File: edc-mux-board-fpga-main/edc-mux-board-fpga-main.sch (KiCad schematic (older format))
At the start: 4 parts

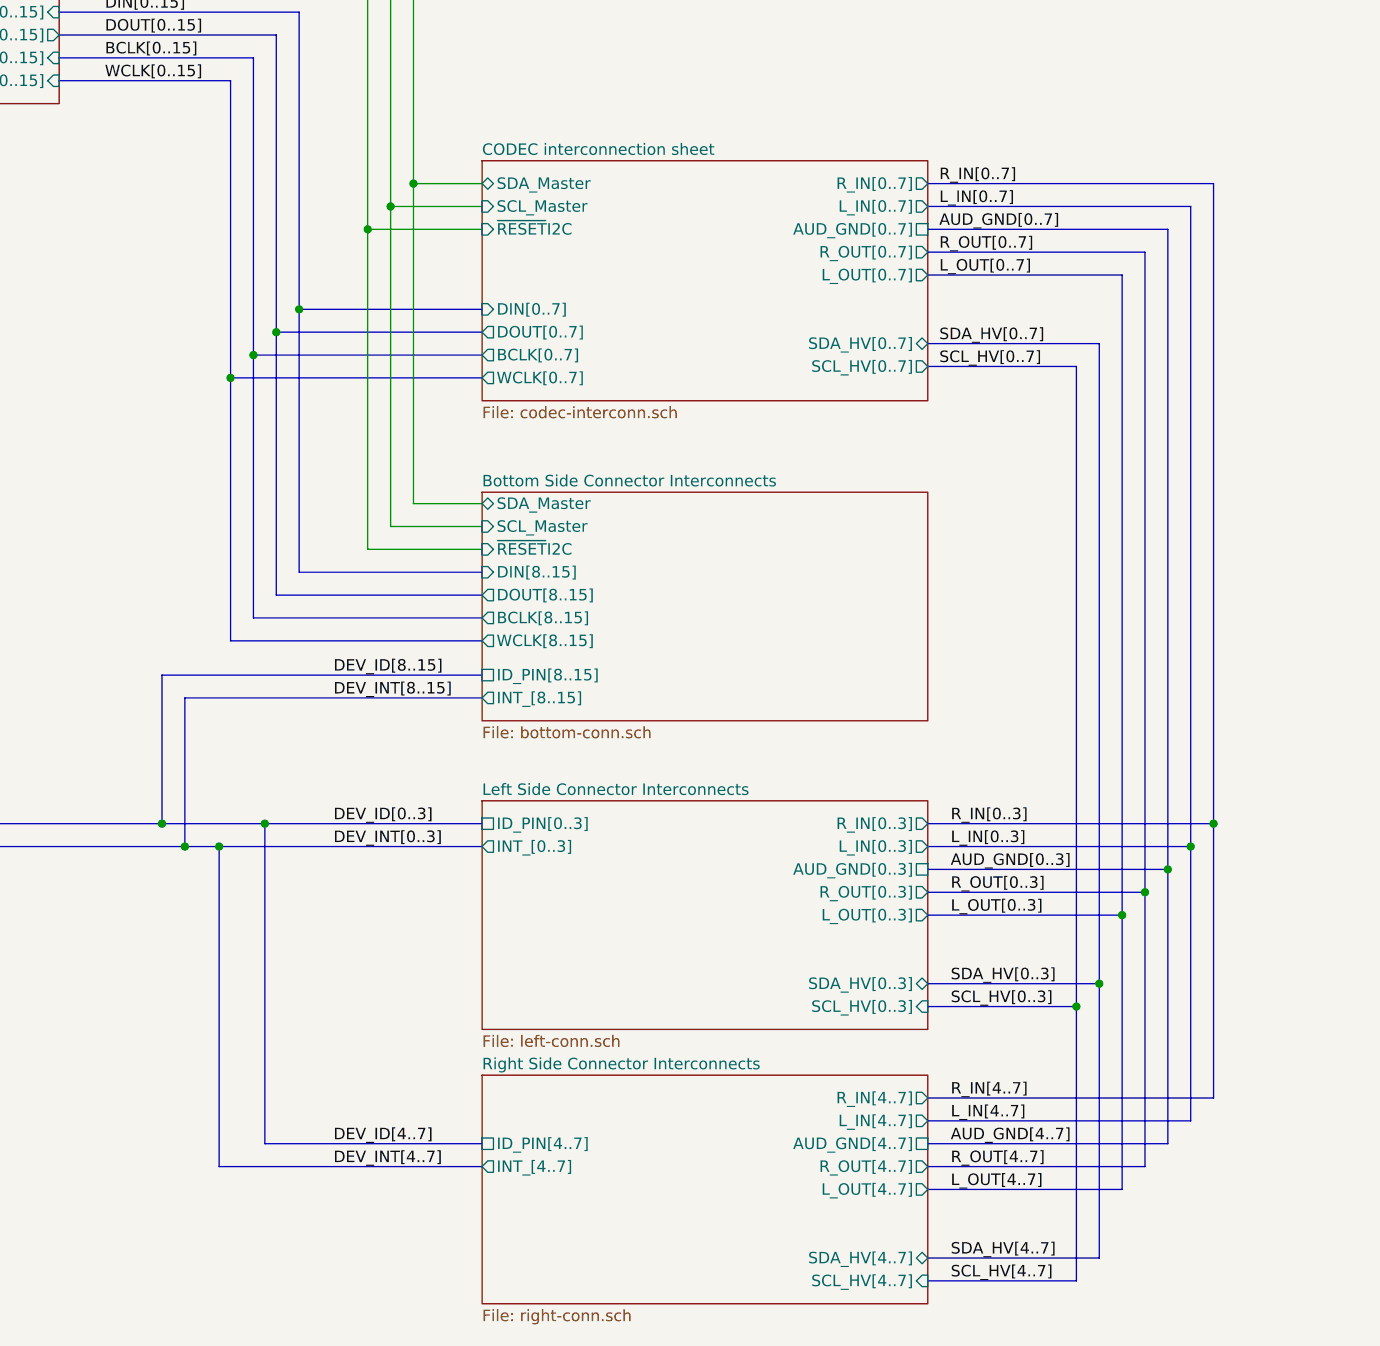
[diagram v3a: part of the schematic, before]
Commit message: testing migration of device connectors and ESD diodes into conn.sch
This means that I can't have the values of the connectors be the device number but hopefully it will allow me to utilize the schematic duplication features with the connectors and diodes
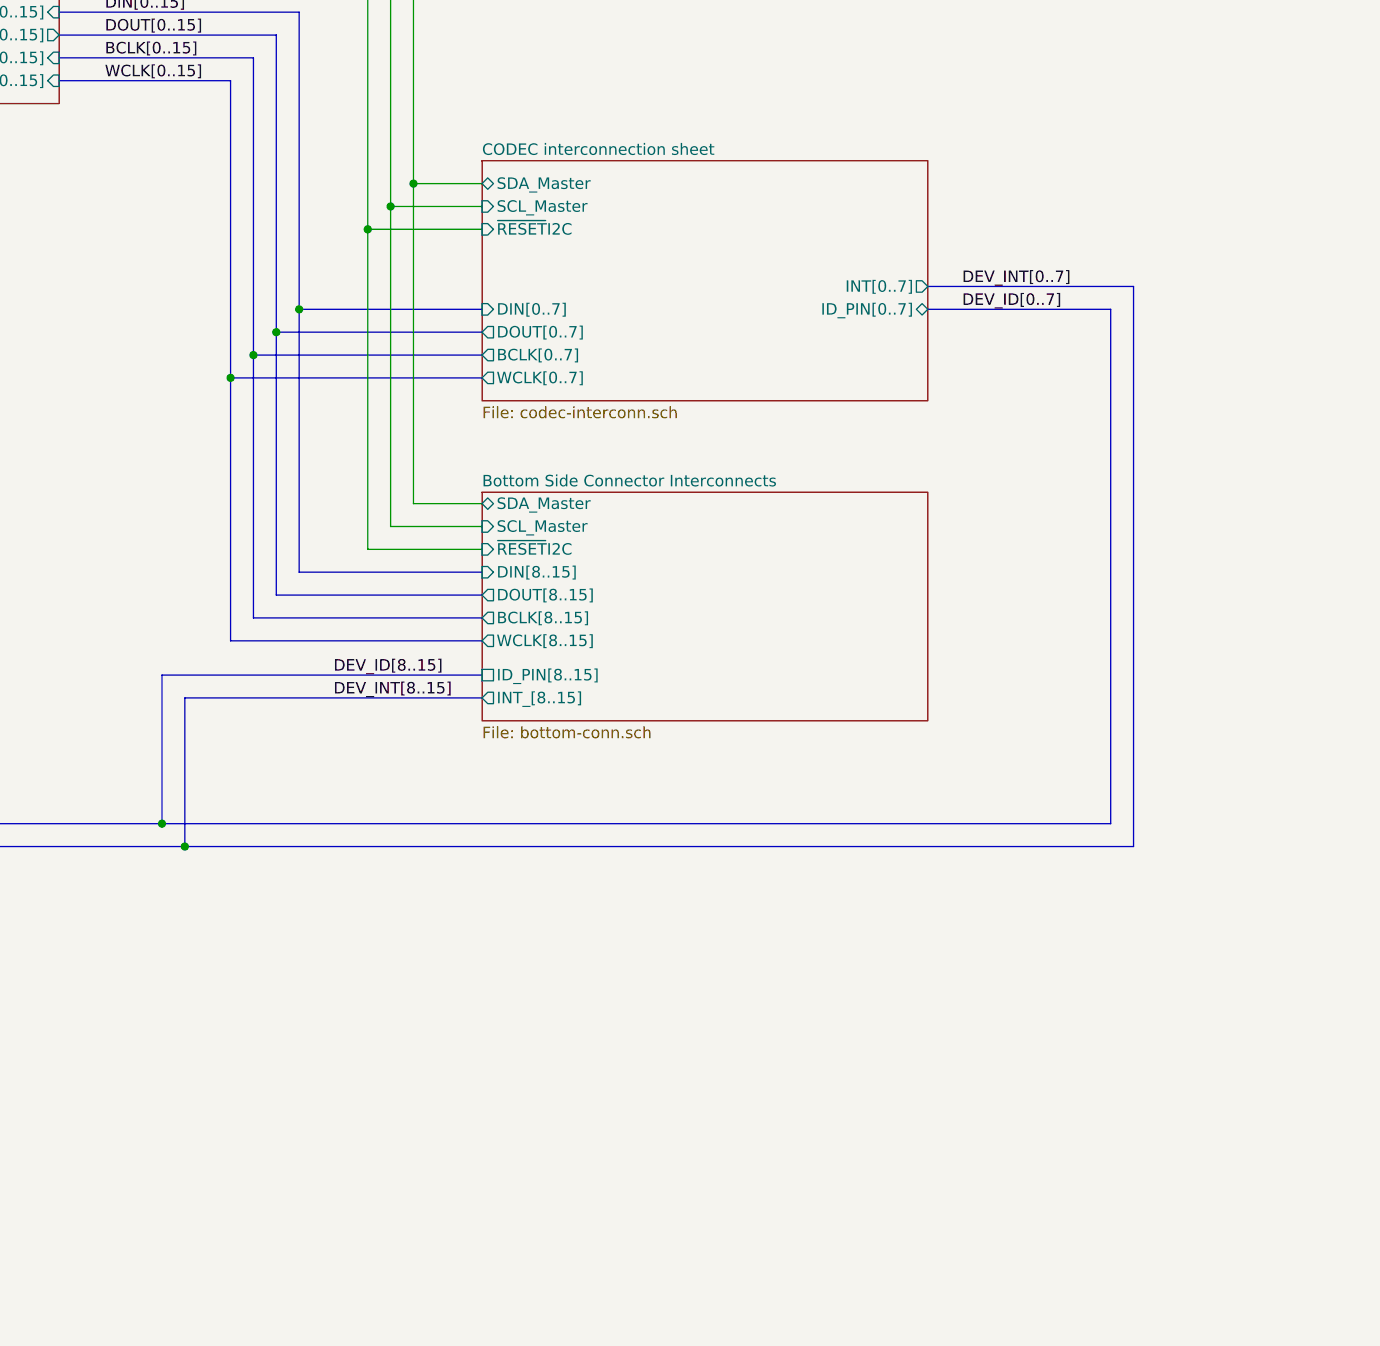
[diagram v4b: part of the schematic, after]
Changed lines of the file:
@@
 $Descr USLedger 17000 11000
 encoding utf-8
-Sheet 1 19
+Sheet 1 17
 Title "EDC Mux Board"
 Date "2019-05-17"
@@
 F4 "BCLK[0..7]" O L 4900 6050 50
 F5 "WCLK[0..7]" O L 4900 6150 50
-F6 "L_OUT[0..7]" O R 6850 5700 50
-F7 "R_OUT[0..7]" O R 6850 5600 50
-F8 "AUD_GND[0..7]" U R 6850 5500 50
-F9 "R_IN[0..7]" O R 6850 5300 50
-F10 "L_IN[0..7]" O R 6850 5400 50
-F11 "SCL_Master" I L 4900 5400 50
-F12 "SDA_Master" B L 4900 5300 50
-F13 "~RESET~I2C" I L 4900 5500 50
-F14 "SDA_HV[0..7]" B R 6850 6000 50
-F15 "SCL_HV[0..7]" O R 6850 6100 50
-$EndSheet
-$Sheet
-S 4900 8000 1950 1000
-U 5CBF625C
-F0 "Left Side Connector Interconnects" 50
-F1 "left-conn.sch" 50
-F2 "R_IN[0..3]" O R 6850 8100 50
-F3 "L_IN[0..3]" O R 6850 8200 50
-F4 "AUD_GND[0..3]" U R 6850 8300 50
-F5 "SDA_HV[0..3]" B R 6850 8800 50
-F6 "SCL_HV[0..3]" I R 6850 8900 50
-F7 "L_OUT[0..3]" O R 6850 8500 50
-F8 "R_OUT[0..3]" O R 6850 8400 50
-F9 "ID_PIN[0..3]" U L 4900 8100 50
-F10 "INT_[0..3]" O L 4900 8200 50
-$EndSheet
-$Sheet
-S 4900 9200 1950 1000
-U 5CBF628A
-F0 "Right Side Connector Interconnects" 50
-F1 "right-conn.sch" 50
-F2 "R_IN[4..7]" O R 6850 9300 50
-F3 "L_IN[4..7]" O R 6850 9400 50
-F4 "AUD_GND[4..7]" U R 6850 9500 50
-F5 "SDA_HV[4..7]" B R 6850 10000 50
-F6 "SCL_HV[4..7]" I R 6850 10100 50
-F7 "L_OUT[4..7]" O R 6850 9700 50
-F8 "R_OUT[4..7]" O R 6850 9600 50
-F9 "ID_PIN[4..7]" U L 4900 9500 50
-F10 "INT_[4..7]" O L 4900 9600 50
+F6 "SCL_Master" I L 4900 5400 50
+F7 "SDA_Master" B L 4900 5300 50
+F8 "~RESET~I2C" I L 4900 5500 50
+F9 "ID_PIN[0..7]" B R 6850 5850 50
+F10 "INT[0..7]" O R 6850 5750 50
 $EndSheet
 Text Notes 17350 6950 0    50   ~ 0
@@
 	3800 6150 4900 6150
 Wire Bus Line
-	6850 5300 8100 5300
-Wire Bus Line
-	6850 5400 8000 5400
-Wire Bus Line
-	6850 5500 7900 5500
-Wire Bus Line
-	6850 5600 7800 5600
-Wire Bus Line
-	6850 5700 7700 5700
-Wire Bus Line
-	6850 6000 7600 6000
-Wire Bus Line
-	6850 6100 7500 6100
-Wire Bus Line
 	900  8100 3500 8100
 Wire Bus Line
@@
 Wire Bus Line
 	800  8200 800  4750
-Text Label 6900 5300 0    50   ~ 0
-R_IN[0..7]
-Text Label 6900 5400 0    50   ~ 0
-L_IN[0..7]
-Text Label 6900 5500 0    50   ~ 0
-AUD_GND[0..7]
-Text Label 6900 5600 0    50   ~ 0
-R_OUT[0..7]
-Text Label 6900 5700 0    50   ~ 0
-L_OUT[0..7]
-Text Label 6900 6000 0    50   ~ 0
-SDA_HV[0..7]
-Text Label 6900 6100 0    50   ~ 0
-SCL_HV[0..7]
-Text Label 6950 8900 0    50   ~ 0
-SCL_HV[0..3]
-Text Label 6950 8800 0    50   ~ 0
-SDA_HV[0..3]
-Text Label 6950 8500 0    50   ~ 0
-L_OUT[0..3]
-Text Label 6950 8400 0    50   ~ 0
-R_OUT[0..3]
-Text Label 6950 8300 0    50   ~ 0
-AUD_GND[0..3]
-Text Label 6950 8200 0    50   ~ 0
-L_IN[0..3]
-Text Label 6950 8100 0    50   ~ 0
-R_IN[0..3]
-Text Label 6950 10100 0    50   ~ 0
-SCL_HV[4..7]
-Text Label 6950 10000 0    50   ~ 0
-SDA_HV[4..7]
-Text Label 6950 9700 0    50   ~ 0
-L_OUT[4..7]
-Text Label 6950 9600 0    50   ~ 0
-R_OUT[4..7]
-Text Label 6950 9500 0    50   ~ 0
-AUD_GND[4..7]
-Text Label 6950 9400 0    50   ~ 0
-L_IN[4..7]
-Text Label 6950 9300 0    50   ~ 0
-R_IN[4..7]
 Text Label 950  4750 0    50   ~ 0
 DEV_INT[0..15]
 Text Label 950  4850 0    50   ~ 0
 DEV_ID[0..15]
-Text Label 4250 8200 0    50   ~ 0
-DEV_INT[0..3]
-Text Label 4250 8100 0    50   ~ 0
-DEV_ID[0..3]
+Text Label 7000 5750 0    50   ~ 0
+DEV_INT[0..7]
+Text Label 7000 5850 0    50   ~ 0
+DEV_ID[0..7]
 Text Label 3250 4550 0    50   ~ 0
 DIN[0..15]
@@
 Connection ~ 3800 6150
 Wire Bus Line
-	3950 8100 3950 9500
-Wire Bus Line
-	3950 9500 4900 9500
-Connection ~ 3950 8100
-Wire Bus Line
-	3950 8100 4900 8100
-Wire Bus Line
-	3750 8200 3750 9600
-Wire Bus Line
-	3750 9600 4900 9600
-Connection ~ 3750 8200
-Wire Bus Line
-	3750 8200 4900 8200
-Text Label 4250 9500 0    50   ~ 0
-DEV_ID[4..7]
-Text Label 4250 9600 0    50   ~ 0
-DEV_INT[4..7]
-Wire Bus Line
 	4900 7450 3500 7450
 Wire Bus Line
@@
 Connection ~ 3500 8100
 Wire Bus Line
-	3500 8100 3950 8100
-Wire Bus Line
 	4900 7550 3600 7550
 Wire Bus Line
 	3600 7550 3600 8200
 Connection ~ 3600 8200
-Wire Bus Line
-	3600 8200 3750 8200
 Text Label 4250 7450 0    50   ~ 0
 DEV_ID[8..15]
 Text Label 4250 7550 0    50   ~ 0
 DEV_INT[8..15]
-Wire Bus Line
-	6850 10100 7500 10100
-Wire Bus Line
-	7500 10100 7500 8900
-Wire Bus Line
-	6850 8900 7500 8900
-Connection ~ 7500 8900
-Wire Bus Line
-	7500 8900 7500 6100
-Wire Bus Line
-	7600 6000 7600 8800
-Wire Bus Line
-	7600 10000 6850 10000
-Wire Bus Line
-	6850 8800 7600 8800
-Connection ~ 7600 8800
-Wire Bus Line
-	7600 8800 7600 10000
-Wire Bus Line
-	7700 5700 7700 8500
-Wire Bus Line
-	7700 9700 6850 9700
-Connection ~ 7700 8500
-Wire Bus Line
-	7700 8500 7700 9700
-Wire Bus Line
-	7800 5600 7800 8400
-Wire Bus Line
-	7800 9600 6850 9600
-Wire Bus Line
-	6850 8400 7800 8400
-Connection ~ 7800 8400
-Wire Bus Line
-	7800 8400 7800 9600
-Wire Bus Line
-	7900 5500 7900 8300
-Wire Bus Line
-	7900 9500 6850 9500
-Wire Bus Line
-	6850 8300 7900 8300
-Connection ~ 7900 8300
-Wire Bus Line
-	7900 8300 7900 9500
-Wire Bus Line
-	8000 5400 8000 8200
-Wire Bus Line
-	8000 9400 6850 9400
-Wire Bus Line
-	6850 8200 8000 8200
-Connection ~ 8000 8200
-Wire Bus Line
-	8000 8200 8000 9400
-Wire Bus Line
-	8100 5300 8100 8100
-Wire Bus Line
-	8100 9300 6850 9300
-Wire Bus Line
-	6850 8100 8100 8100
-Connection ~ 8100 8100
-Wire Bus Line
-	8100 8100 8100 9300
-Wire Bus Line
-	6850 8500 7700 8500
 $Sheet
 S 7300 3300 2550 1100
@@
 F7 "~INT" O L 7300 3900 50
 $EndSheet
+Wire Bus Line
+	7650 8100 7650 5850
+Wire Bus Line
+	7650 5850 6850 5850
+Wire Bus Line
+	3500 8100 7650 8100
+Wire Bus Line
+	7750 8200 7750 5750
+Wire Bus Line
+	7750 5750 6850 5750
+Wire Bus Line
+	3600 8200 7750 8200
 $EndSCHEMATC

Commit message: Some minor fixes
- swapped 5Ω resistors to 4.99Ω resistors so I could actually buy them
- swapped power switch connector over to a JST PH connector like the rest of the connectors.
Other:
- moved on the sheet: H1, H2, H3, H4
